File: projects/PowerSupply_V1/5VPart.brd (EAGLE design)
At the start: 50 x 50 mm, 26 parts, among them IC1 LM2596T, IC2 LM2596T, X1 IN, X2 OUT

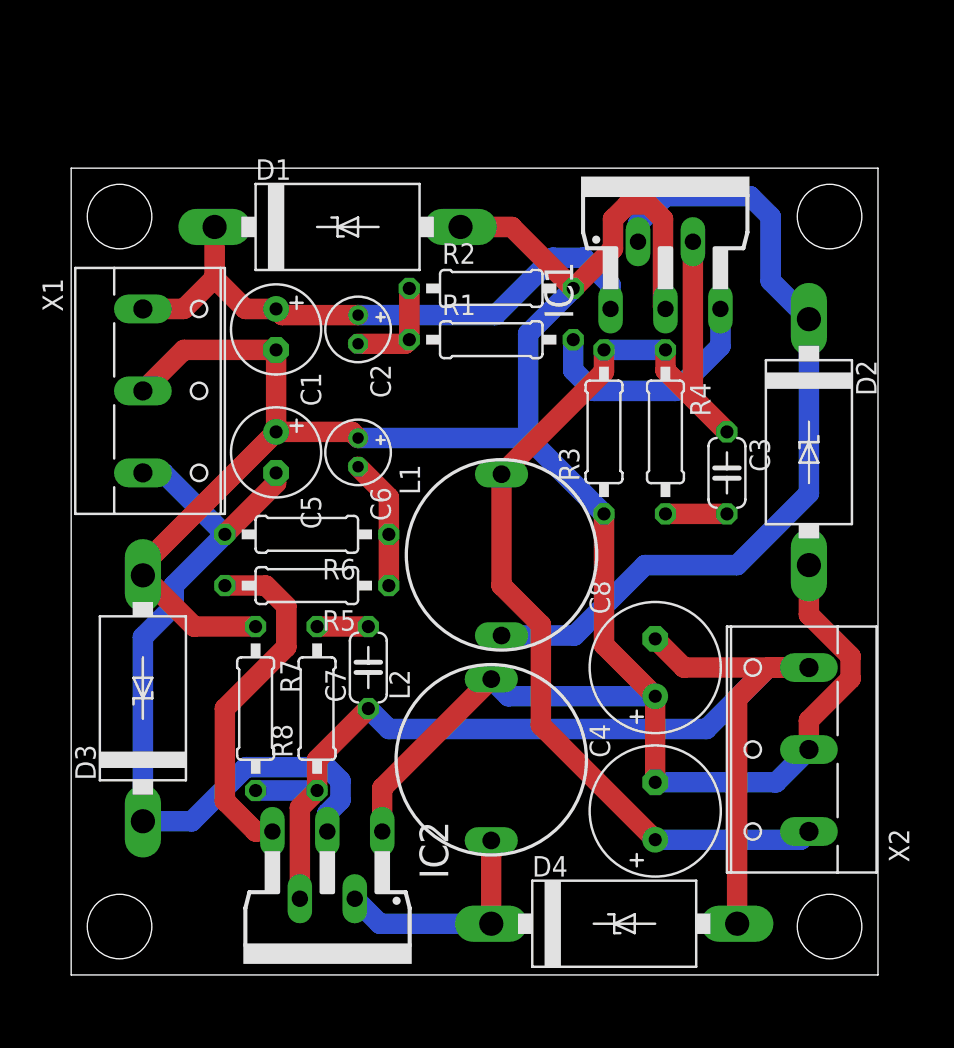
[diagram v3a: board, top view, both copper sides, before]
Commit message: feat: 5VPart refactored
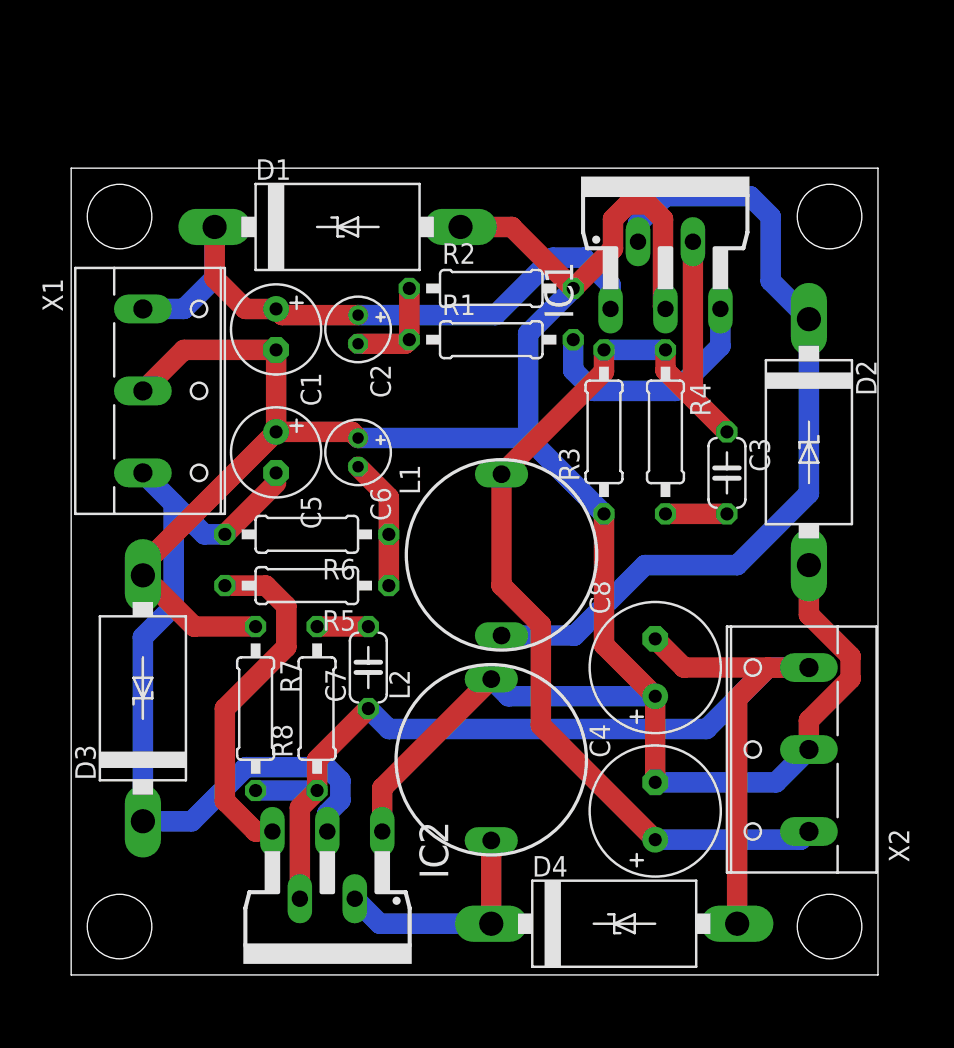
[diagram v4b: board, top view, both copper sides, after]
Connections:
- net +24V renamed +20V
- net -24V renamed -20V
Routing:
- net +20V: track 38.2 -> 41.4 mm
- net -5V: track 76.2 -> 73.7 mm
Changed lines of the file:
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@@
 <wire x1="36.83" y1="28.575" x2="40.64" y2="28.575" width="1.27" layer="1"/>
-</signal>
-<signal name="+24V">
-<contactref element="X1" pad="1"/>
-<contactref element="C1" pad="+"/>
-<contactref element="IC1" pad="1"/>
-<contactref element="C2" pad="+"/>
-<contactref element="D1" pad="C"/>
-<wire x1="8.89" y1="45.72" x2="8.89" y2="46.355" width="1.27" layer="1"/>
-<wire x1="8.89" y1="43.18" x2="10.795" y2="41.275" width="1.27" layer="1"/>
-<wire x1="10.795" y1="41.275" x2="12.7" y2="41.275" width="1.27" layer="1"/>
-<wire x1="8.89" y1="46.355" x2="8.89" y2="43.18" width="1.27" layer="1"/>
-<wire x1="4.445" y1="41.275" x2="6.985" y2="41.275" width="1.27" layer="1"/>
-<wire x1="6.985" y1="41.275" x2="8.89" y2="43.18" width="1.27" layer="1"/>
-<wire x1="17.78" y1="40.894" x2="13.081" y2="40.894" width="1.27" layer="1"/>
-<wire x1="13.081" y1="40.894" x2="12.7" y2="41.275" width="1.27" layer="1"/>
-<wire x1="17.78" y1="40.894" x2="26.289" y2="40.894" width="1.27" layer="16"/>
-<wire x1="26.289" y1="40.894" x2="29.845" y2="44.45" width="1.27" layer="16"/>
-<wire x1="29.845" y1="44.45" x2="31.75" y2="44.45" width="1.27" layer="16"/>
-<wire x1="31.75" y1="44.45" x2="33.4264" y2="42.7736" width="1.27" layer="16"/>
-<wire x1="33.4264" y1="42.7736" x2="33.4264" y2="41.275" width="1.27" layer="16"/>
-</signal>
-<signal name="-24V">
-<contactref element="C5" pad="-"/>
-<contactref element="R6" pad="2"/>
-<contactref element="IC2" pad="3"/>
-<contactref element="D3" pad="C"/>
-<contactref element="X1" pad="3"/>
-<wire x1="9.525" y1="27.305" x2="12.7" y2="30.48" width="1.27" layer="1"/>
-<wire x1="12.7" y1="30.48" x2="12.7" y2="31.115" width="1.27" layer="1"/>
-<wire x1="16.6878" y1="10.8303" x2="16.6878" y2="12.0297" width="1.27" layer="16"/>
-<wire x1="16.6878" y1="12.0297" x2="15.8397" y2="12.8778" width="1.27" layer="16"/>
-<wire x1="7.4775" y1="9.525" x2="4.445" y2="9.525" width="1.27" layer="16"/>
-<wire x1="15.8397" y1="12.8778" x2="10.8303" y2="12.8778" width="1.27" layer="16"/>
-<wire x1="10.8303" y1="12.8778" x2="7.4775" y2="9.525" width="1.27" layer="16"/>
-<wire x1="15.875" y1="8.89" x2="15.875" y2="10.0175" width="1.27" layer="16"/>
-<wire x1="15.875" y1="10.0175" x2="16.6878" y2="10.8303" width="1.27" layer="16"/>
-<wire x1="4.445" y1="31.115" x2="5.715" y2="31.115" width="1.27" layer="16"/>
-<wire x1="5.715" y1="31.115" x2="9.525" y2="27.305" width="1.27" layer="16"/>
-<wire x1="9.525" y1="27.305" x2="6.35635" y2="24.13635" width="1.27" layer="16"/>
-<wire x1="6.35635" y1="24.13635" x2="6.35635" y2="22.8493375" width="1.27" layer="16"/>
-<wire x1="4.445" y1="20.9379875" x2="4.445" y2="9.525" width="1.27" layer="16"/>
-<wire x1="6.35635" y1="22.8493375" x2="4.445" y2="20.9379875" width="1.27" layer="16"/>
 </signal>
 <signal name="N$4">
@@
 </signal>
 <signal name="+5V">
-<contactref element="X2" pad="1"/>
 <contactref element="R3" pad="2"/>
 <contactref element="IC1" pad="4"/>
@@
 <wire x1="29.1074" y1="21.70288125" x2="29.1074" y2="15.4696" width="1.27" layer="1"/>
 <wire x1="33.02" y1="38.735" x2="36.83" y2="38.735" width="1.27" layer="16"/>
-<wire x1="36.195" y1="8.382" x2="45.212" y2="8.382" width="1.27" layer="16"/>
-<wire x1="45.212" y1="8.382" x2="45.72" y2="8.89" width="1.27" layer="16"/>
+<contactref element="X2" pad="1"/>
+<wire x1="45.72" y1="8.89" x2="45.212" y2="8.382" width="1.27" layer="16"/>
+<wire x1="45.212" y1="8.382" x2="36.195" y2="8.382" width="1.27" layer="16"/>
 </signal>
 <signal name="-5V">
-<contactref element="X2" pad="3"/>
 <contactref element="C8" pad="-"/>
 <contactref element="IC2" pad="4"/>
@@
 <wire x1="15.24" y1="13.335" x2="18.415" y2="16.51" width="1.27" layer="1"/>
 <wire x1="11.43" y1="11.43" x2="15.24" y2="11.43" width="1.27" layer="16"/>
-<wire x1="18.415" y1="16.51" x2="19.685" y2="15.24" width="1.27" layer="16"/>
-<wire x1="41.275" y1="3.175" x2="41.275" y2="17.145" width="1.27" layer="1"/>
+<contactref element="X2" pad="3"/>
+<wire x1="39.37" y1="15.24" x2="19.685" y2="15.24" width="1.27" layer="16"/>
+<wire x1="37.973" y1="19.05" x2="43.18" y2="19.05" width="1.27" layer="1"/>
+<wire x1="43.18" y1="19.05" x2="45.72" y2="19.05" width="1.27" layer="1"/>
 <wire x1="41.275" y1="17.145" x2="43.18" y2="19.05" width="1.27" layer="1"/>
-<wire x1="43.18" y1="19.05" x2="45.72" y2="19.05" width="1.27" layer="1"/>
-<wire x1="45.72" y1="19.05" x2="37.973" y2="19.05" width="1.27" layer="1"/>
-<wire x1="37.973" y1="19.05" x2="36.195" y2="20.828" width="1.27" layer="1"/>
 <wire x1="39.37" y1="15.24" x2="43.18" y2="19.05" width="1.27" layer="16"/>
 <wire x1="43.18" y1="19.05" x2="45.72" y2="19.05" width="1.27" layer="16"/>
-<wire x1="19.685" y1="15.24" x2="39.37" y2="15.24" width="1.27" layer="16"/>
+<wire x1="36.195" y1="20.828" x2="37.973" y2="19.05" width="1.27" layer="1"/>
+<wire x1="41.275" y1="3.175" x2="41.275" y2="17.145" width="1.27" layer="1"/>
+<wire x1="19.685" y1="15.24" x2="18.415" y2="16.51" width="1.27" layer="16"/>
+</signal>
+<signal name="+20V">
+<contactref element="X1" pad="1"/>
+<contactref element="C1" pad="+"/>
+<contactref element="IC1" pad="1"/>
+<contactref element="C2" pad="+"/>
+<contactref element="D1" pad="C"/>
+<wire x1="8.89" y1="45.72" x2="8.89" y2="46.355" width="1.27" layer="1"/>
+<wire x1="8.89" y1="43.18" x2="10.795" y2="41.275" width="1.27" layer="1"/>
+<wire x1="10.795" y1="41.275" x2="12.7" y2="41.275" width="1.27" layer="1"/>
+<wire x1="8.89" y1="46.355" x2="8.89" y2="43.18" width="1.27" layer="1"/>
+<wire x1="17.78" y1="40.894" x2="13.081" y2="40.894" width="1.27" layer="1"/>
+<wire x1="13.081" y1="40.894" x2="12.7" y2="41.275" width="1.27" layer="1"/>
+<wire x1="17.78" y1="40.894" x2="26.289" y2="40.894" width="1.27" layer="16"/>
+<wire x1="26.289" y1="40.894" x2="29.845" y2="44.45" width="1.27" layer="16"/>
+<wire x1="29.845" y1="44.45" x2="31.75" y2="44.45" width="1.27" layer="16"/>
+<wire x1="31.75" y1="44.45" x2="33.4264" y2="42.7736" width="1.27" layer="16"/>
+<wire x1="33.4264" y1="42.7736" x2="33.4264" y2="41.275" width="1.27" layer="16"/>
+<wire x1="8.89" y1="46.355" x2="8.89" y2="43.18" width="1.27" layer="16"/>
+<wire x1="8.89" y1="43.18" x2="6.985" y2="41.275" width="1.27" layer="16"/>
+<wire x1="6.985" y1="41.275" x2="4.445" y2="41.275" width="1.27" layer="16"/>
+</signal>
+<signal name="-20V">
+<contactref element="X1" pad="3"/>
+<contactref element="D3" pad="C"/>
+<contactref element="R6" pad="2"/>
+<contactref element="IC2" pad="3"/>
+<wire x1="16.6878" y1="10.8303" x2="16.6878" y2="12.0297" width="1.27" layer="16"/>
+<wire x1="16.6878" y1="12.0297" x2="15.8397" y2="12.8778" width="1.27" layer="16"/>
+<wire x1="15.8397" y1="12.8778" x2="10.8303" y2="12.8778" width="1.27" layer="16"/>
+<wire x1="10.8303" y1="12.8778" x2="7.4775" y2="9.525" width="1.27" layer="16"/>
+<wire x1="15.875" y1="8.89" x2="15.875" y2="10.0175" width="1.27" layer="16"/>
+<wire x1="15.875" y1="10.0175" x2="16.6878" y2="10.8303" width="1.27" layer="16"/>
+<wire x1="4.445" y1="20.9379875" x2="6.35635" y2="22.8493375" width="1.27" layer="16"/>
+<wire x1="9.525" y1="27.305" x2="12.7" y2="30.48" width="1.27" layer="1"/>
+<contactref element="C5" pad="-"/>
+<wire x1="4.445" y1="20.9379875" x2="4.445" y2="9.525" width="1.27" layer="16"/>
+<wire x1="7.4775" y1="9.525" x2="4.445" y2="9.525" width="1.27" layer="16"/>
+<wire x1="4.445" y1="31.115" x2="6.35635" y2="29.20365" width="1.27" layer="16"/>
+<wire x1="6.35635" y1="22.8493375" x2="6.35635" y2="29.20365" width="1.27" layer="16"/>
+<wire x1="6.35635" y1="29.20365" x2="8.255" y2="27.305" width="1.27" layer="16"/>
+<wire x1="8.255" y1="27.305" x2="9.525" y2="27.305" width="1.27" layer="16"/>
+<wire x1="12.7" y1="30.48" x2="12.7" y2="31.115" width="0" layer="19" extent="1-1"/>
 </signal>
 </signals>

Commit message: feat: small fixes and changes applied
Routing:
- net -5V: track 73.7 -> 74.5 mm
